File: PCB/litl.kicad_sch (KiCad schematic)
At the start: 101 parts, among them J1 Conn_01x04, SW1 KEYSW, SW10 KEYSW, SW11 KEYSW, SW12 KEYSW, SW13 KEYSW, SW14 KEYSW, SW15 KEYSW, SW16 KEYSW, SW17 KEYSW, SW18 KEYSW, SW19 KEYSW, SW2 KEYSW, SW20 KEYSW, SW21 KEYSW, SW22 KEYSW, SW23 KEYSW, SW24 KEYSW, SW25 KEYSW, SW26 KEYSW, SW27 KEYSW, SW28 KEYSW, SW29 KEYSW, SW3 KEYSW, SW30 KEYSW, SW31 KEYSW, SW32 KEYSW, SW33 KEYSW, SW34 KEYSW, SW35 KEYSW, SW36 KEYSW, SW37 KEYSW, SW38 KEYSW, SW39 KEYSW, SW4 KEYSW, SW40 KEYSW, SW41 KEYSW, SW42 KEYSW, SW43 KEYSW, SW44 KEYSW, SW45 KEYSW, SW46 KEYSW, SW47 KEYSW, SW48 KEYSW, SW49 KEYSW, SW5 KEYSW, SW50 KEYSW, SW51 RotaryEncoder_Switch, SW53 RotaryEncoder_Switch, SW6 KEYSW, SW7 KEYSW, SW8 KEYSW, SW9 KEYSW, U1 ProMicro

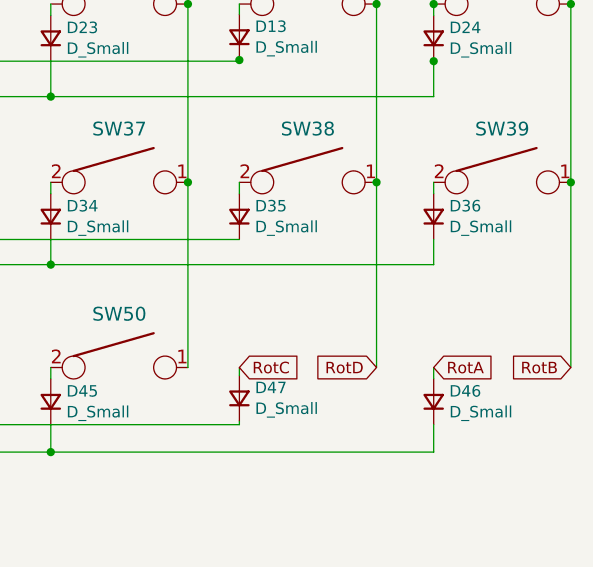
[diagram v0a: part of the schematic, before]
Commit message: Updated silkscreening on board and switch socket option added for encoders. Gerbers v2.1 added
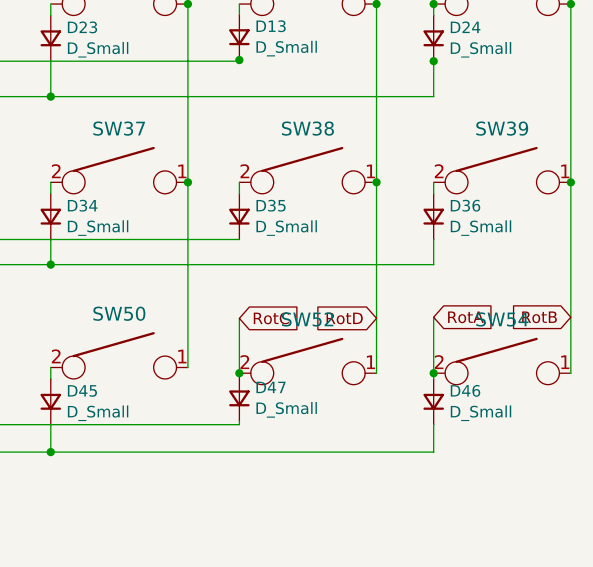
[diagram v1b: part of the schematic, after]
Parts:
- added SW52, SW54: KEYSW, Button_Switch_Keyboard:SW_Cherry_MX_1.25u_PCB, symbol keyboard_parts:KEYSW
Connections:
- net RotA: now also SW54.2
- net RotB: now also SW52.1, SW54.1
- net RotC: now also SW52.2
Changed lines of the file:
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@@
   (junction (at 229.235 38.735) (diameter 0) (color 0 0 0 0)
   )
+  (junction (at 257.175 100.33) (diameter 0) (color 0 0 0 0)
+  )
   (junction (at 213.995 65.659) (diameter 0) (color 0 0 0 0)
   )
@@
   (junction (at 148.59 69.596) (diameter 0) (color 0 0 0 0)
   )
+  (junction (at 278.765 100.33) (diameter 0) (color 0 0 0 0)
+  )
   (junction (at 192.405 109.093) (diameter 0) (color 0 0 0 0)
   )
@@
     (stroke (width 0) (type default) (color 0 0 0 0))
   )
+  (wire (pts (xy 278.765 100.33) (xy 278.765 100.965))
+    (stroke (width 0) (type default) (color 0 0 0 0))
+  )
   (wire (pts (xy 148.59 45.085) (xy 148.59 48.387))
     (stroke (width 0) (type default) (color 0 0 0 0))
@@
     (stroke (width 0) (type default) (color 0 0 0 0))
   )
-  (wire (pts (xy 278.765 99.695) (xy 278.765 100.965))
+  (wire (pts (xy 278.765 94.107) (xy 278.765 100.33))
     (stroke (width 0) (type default) (color 0 0 0 0))
   )
@@
     (stroke (width 0) (type default) (color 0 0 0 0))
   )
-  (wire (pts (xy 272.415 79.121) (xy 272.415 99.695))
+  (wire (pts (xy 272.415 79.121) (xy 272.415 100.33))
     (stroke (width 0) (type default) (color 0 0 0 0))
   )
@@
     (stroke (width 0) (type default) (color 0 0 0 0))
   )
-  (wire (pts (xy 257.175 99.695) (xy 257.175 100.584))
+  (wire (pts (xy 257.175 94.234) (xy 257.175 100.33))
     (stroke (width 0) (type default) (color 0 0 0 0))
   )
@@
     (stroke (width 0) (type default) (color 0 0 0 0))
   )
-  (wire (pts (xy 294.005 79.121) (xy 294.005 99.695))
+  (wire (pts (xy 294.005 79.121) (xy 294.005 100.33))
     (stroke (width 0) (type default) (color 0 0 0 0))
   )
@@
     (stroke (width 0) (type default) (color 0 0 0 0))
   )
+  (wire (pts (xy 257.175 100.33) (xy 257.175 100.584))
+    (stroke (width 0) (type default) (color 0 0 0 0))
+  )
   (wire (pts (xy 121.285 59.309) (xy 121.285 79.121))
     (stroke (width 0) (type default) (color 0 0 0 0))
@@
     )
   )
-  (global_label "RotD" (shape input) (at 272.415 99.695 180) (fields_autoplaced)
+  (global_label "RotD" (shape input) (at 272.415 94.234 180) (fields_autoplaced)
     (effects (font (size 1.27 1.27)) (justify right))
-    (property "Intersheet References" "${INTERSHEET_REFS}" (id 0) (at 265.5871 99.6156 0)
+    (property "Intersheet References" "${INTERSHEET_REFS}" (id 0) (at 265.5871 94.1546 0)
       (effects (font (size 1.27 1.27)) (justify right) hide)
     )
@@
     )
   )
-  (global_label "RotC" (shape input) (at 257.175 99.695 0) (fields_autoplaced)
+  (global_label "RotC" (shape input) (at 257.175 94.234 0) (fields_autoplaced)
     (effects (font (size 1.27 1.27)) (justify left))
-    (property "Intersheet References" "${INTERSHEET_REFS}" (id 0) (at 264.0029 99.6156 0)
+    (property "Intersheet References" "${INTERSHEET_REFS}" (id 0) (at 264.0029 94.1546 0)
       (effects (font (size 1.27 1.27)) (justify left) hide)
     )
@@
     )
   )
-  (global_label "RotB" (shape input) (at 294.005 99.695 180) (fields_autoplaced)
+  (global_label "RotB" (shape input) (at 294.005 94.107 180) (fields_autoplaced)
     (effects (font (size 1.27 1.27)) (justify right))
-    (property "Intersheet References" "${INTERSHEET_REFS}" (id 0) (at 287.1771 99.7744 0)
+    (property "Intersheet References" "${INTERSHEET_REFS}" (id 0) (at 287.1771 94.1864 0)
       (effects (font (size 1.27 1.27)) (justify right) hide)
     )
@@
     )
   )
-  (global_label "RotA" (shape input) (at 278.765 99.695 0) (fields_autoplaced)
+  (global_label "RotA" (shape input) (at 278.765 94.107 0) (fields_autoplaced)
     (effects (font (size 1.27 1.27)) (justify left))
-    (property "Intersheet References" "${INTERSHEET_REFS}" (id 0) (at 285.4114 99.6156 0)
+    (property "Intersheet References" "${INTERSHEET_REFS}" (id 0) (at 285.4114 94.0276 0)
       (effects (font (size 1.27 1.27)) (justify left) hide)
     )
@@
     (pin "2")
   )
+  (symbol (lib_id "keyboard_parts:KEYSW") (at 264.795 100.33 0) (unit 1)
+    (in_bom yes) (on_board yes)
+    (property "Reference" "SW52" (id 0) (at 264.795 94.4118 0)
+      (effects (font (size 1.524 1.524)))
+    )
+    (property "Value" "KEYSW" (id 1) (at 264.795 102.87 0)
+      (effects (font (size 1.524 1.524)) hide)
+    )
+    (property "Footprint" "Button_Switch_Keyboard:SW_Cherry_MX_1.25u_PCB" (id 2) (at 264.795 100.33 0)
+      (effects (font (size 1.524 1.524)) hide)
+    )
+    (property "Datasheet" "" (id 3) (at 264.795 100.33 0)
+      (effects (font (size 1.524 1.524)))
+    )
+    (pin "1")
+    (pin "2")
+  )
   (symbol (lib_id "keyboard_parts:KEYSW") (at 50.165 59.309 0) (unit 1)
     (in_bom yes) (on_board yes)
@@
     (pin "2")
   )
+  (symbol (lib_id "keyboard_parts:KEYSW") (at 286.385 100.33 0) (unit 1)
+    (in_bom yes) (on_board yes)
+    (property "Reference" "SW54" (id 0) (at 286.385 94.4118 0)
+      (effects (font (size 1.524 1.524)))
+    )
+    (property "Value" "KEYSW" (id 1) (at 286.385 102.87 0)
+      (effects (font (size 1.524 1.524)) hide)
+    )
+    (property "Footprint" "Button_Switch_Keyboard:SW_Cherry_MX_1.25u_PCB" (id 2) (at 286.385 100.33 0)
+      (effects (font (size 1.524 1.524)) hide)
+    )
+    (property "Datasheet" "" (id 3) (at 286.385 100.33 0)
+      (effects (font (size 1.524 1.524)))
+    )
+    (pin "1")
+    (pin "2")
+  )
   (symbol (lib_id "keebio:ProMicro") (at 62.23 166.243 0) (unit 1)
     (in_bom yes) (on_board yes) (fields_autoplaced)
@@
       (reference "SW51") (unit 1) (value "RotaryEncoder_Switch") (footprint "Keebio-Parts:RotaryEncoder_EC11")
     )
+    (path "/323166a4-910a-417b-8c7d-c03feb7ffad4"
+      (reference "SW52") (unit 1) (value "KEYSW") (footprint "Button_Switch_Keyboard:SW_Cherry_MX_1.25u_PCB")
+    )
     (path "/9f2ed50d-6137-4ef3-87c1-facccc3023ec"
       (reference "SW53") (unit 1) (value "RotaryEncoder_Switch") (footprint "Keebio-Parts:RotaryEncoder_EC11")
     )
+    (path "/d6f2afd5-5063-490a-877e-a2d97d208be0"
+      (reference "SW54") (unit 1) (value "KEYSW") (footprint "Button_Switch_Keyboard:SW_Cherry_MX_1.25u_PCB")
+    )
     (path "/d7bfc220-64e9-4c8a-a8dd-fca0327e1f71"

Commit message: Litl v3 created
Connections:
- net RotA: now also SW51.S2; no longer SW51.S1
- net RotB: now also SW51.S1, SW53.S1; no longer SW51.S2, SW53.S2
- net RotC: now also SW53.S2; no longer SW53.S1
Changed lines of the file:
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@@
     )
   )
-  (global_label "RotD" (shape input) (at 183.388 140.335 0) (fields_autoplaced)
+  (global_label "RotD" (shape input) (at 183.388 135.255 0) (fields_autoplaced)
     (effects (font (size 1.27 1.27)) (justify left))
-    (property "Intersheet References" "${INTERSHEET_REFS}" (id 0) (at 190.2159 140.2556 0)
+    (property "Intersheet References" "${INTERSHEET_REFS}" (id 0) (at 190.2159 135.1756 0)
       (effects (font (size 1.27 1.27)) (justify left) hide)
     )
@@
     )
   )
-  (global_label "RotA" (shape input) (at 142.494 134.874 0) (fields_autoplaced)
+  (global_label "RotA" (shape input) (at 142.494 139.954 0) (fields_autoplaced)
     (effects (font (size 1.27 1.27)) (justify left))
-    (property "Intersheet References" "${INTERSHEET_REFS}" (id 0) (at 149.1404 134.7946 0)
+    (property "Intersheet References" "${INTERSHEET_REFS}" (id 0) (at 149.1404 139.8746 0)
       (effects (font (size 1.27 1.27)) (justify left) hide)
     )
@@
     )
   )
-  (global_label "RotC" (shape input) (at 183.388 135.255 0) (fields_autoplaced)
+  (global_label "RotC" (shape input) (at 183.388 140.335 0) (fields_autoplaced)
     (effects (font (size 1.27 1.27)) (justify left))
-    (property "Intersheet References" "${INTERSHEET_REFS}" (id 0) (at 190.2159 135.1756 0)
+    (property "Intersheet References" "${INTERSHEET_REFS}" (id 0) (at 190.2159 140.2556 0)
       (effects (font (size 1.27 1.27)) (justify left) hide)
     )
@@
     )
   )
-  (global_label "RotB" (shape input) (at 142.494 139.954 0) (fields_autoplaced)
+  (global_label "RotB" (shape input) (at 142.494 134.874 0) (fields_autoplaced)
     (effects (font (size 1.27 1.27)) (justify left))
-    (property "Intersheet References" "${INTERSHEET_REFS}" (id 0) (at 149.3219 139.8746 0)
+    (property "Intersheet References" "${INTERSHEET_REFS}" (id 0) (at 149.3219 134.7946 0)
       (effects (font (size 1.27 1.27)) (justify left) hide)
     )
